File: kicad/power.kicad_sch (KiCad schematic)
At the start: 48 parts, among them J5 Conn_Coaxial_Power, J6 Screw_Terminal_01x02, U11 ADP7118ACPZN, U22 ADP7118ACPZN, U23 LTM8074EY-PBF, U7 LTM8078EY-PBF, U8 ADP7118ACPZN, U9 ADP7118ACPZN

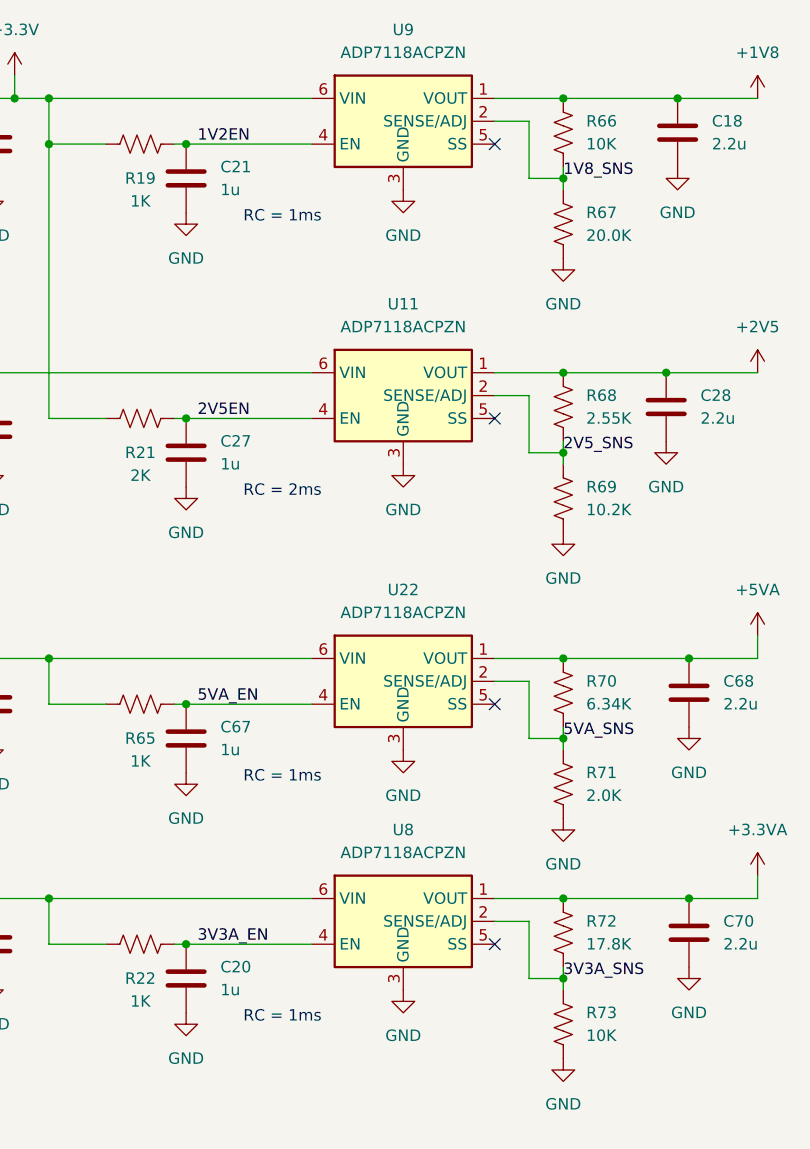
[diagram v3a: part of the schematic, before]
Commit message: fix adc_clk, adp7118
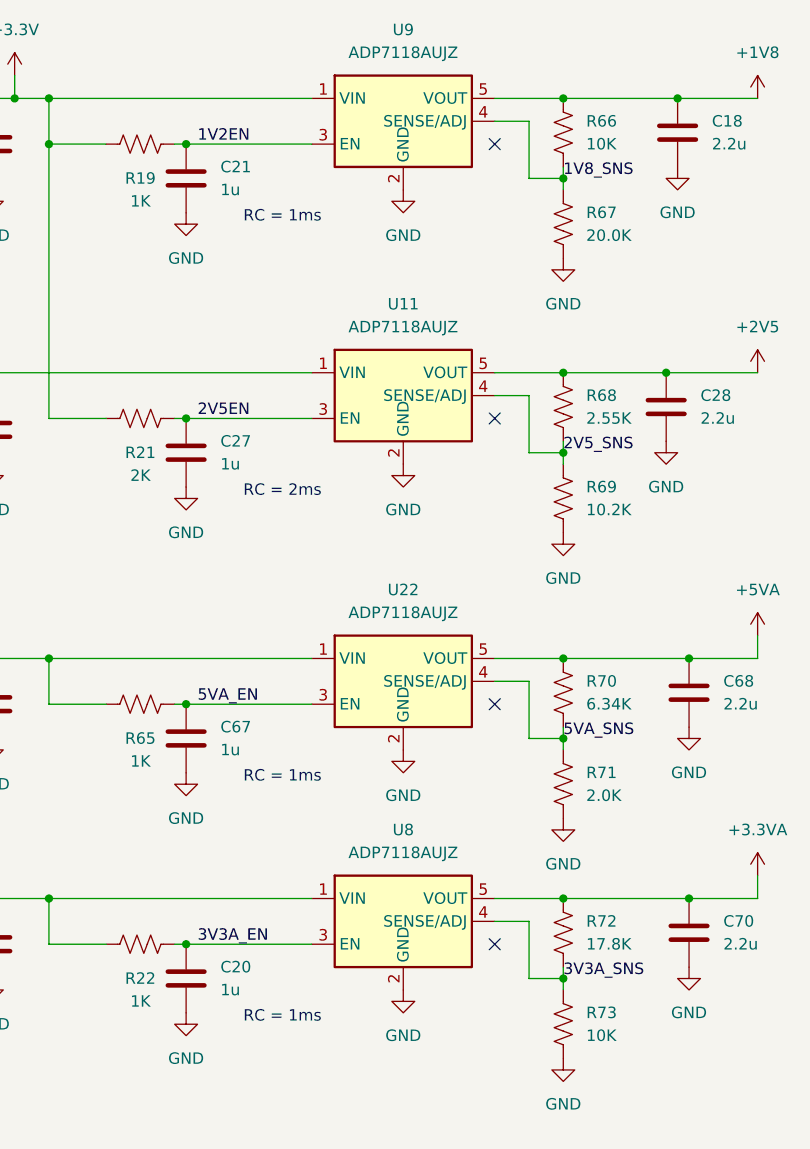
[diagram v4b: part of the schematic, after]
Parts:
- U11, U22, U8, U9: value ADP7118ACPZN -> ADP7118AUJZ; footprint Package_CSP:LFCSP-6-1EP_2x2mm_P0.65mm_EP1x1.6mm -> bgelb_footprint:UJ_5_ADI; symbol Regulator_Linear:ADP7118ACPZN -> bgelb_lib:ADP7118AUJZ
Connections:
- net +1V8: now also U9.5 (VOUT); no longer U9.1 (VOUT)
- net +2V5: now also U11.5 (VOUT); no longer U11.1 (VOUT)
- net +3.3V: now also U11.1 (VIN), U9.1 (VIN); no longer U11.6 (VIN), U9.6 (VIN)
- net +3.3VA: now also U8.5 (VOUT); no longer U8.1 (VOUT)
- net +5VA: now also U22.5 (VOUT); no longer U22.1 (VOUT)
- net 1V2EN: now also U9.3 (EN); no longer U9.4 (EN)
- net 1V8_SNS: now also U9.4 (SENSE/ADJ); no longer U9.2 (SENSE/ADJ)
- net 2V5EN: now also U11.3 (EN); no longer U11.4 (EN)
- net 2V5_SNS: now also U11.4 (SENSE/ADJ); no longer U11.2 (SENSE/ADJ)
- net 3V3A_EN: now also U8.3 (EN); no longer U8.4 (EN)
- net 3V3A_SNS: now also U8.4 (SENSE/ADJ); no longer U8.2 (SENSE/ADJ)
- net 5V5_OUT: now also U22.1 (VIN), U8.1 (VIN); no longer U22.6 (VIN), U8.6 (VIN)
- net 5VA_EN: now also U22.3 (EN); no longer U22.4 (EN)
- net 5VA_SNS: now also U22.4 (SENSE/ADJ); no longer U22.2 (SENSE/ADJ)
- net GND: now also U11.2 (GND), U22.2 (GND), U8.2 (GND), U9.2 (GND); no longer U11.3 (GND), U11.7 (GND), U22.3 (GND), U22.7 (GND), U8.3 (GND), U8.7 (GND), U9.3 (GND), U9.7 (GND)
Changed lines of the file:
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@@
     )
   )
-  (symbol (lib_id "Regulator_Linear:ADP7118ACPZN") (at 302.26 59.69 0) (unit 1)
+  (symbol (lib_id "bgelb_lib:ADP7118AUJZ") (at 302.26 59.69 0) (unit 1)
     (in_bom yes) (on_board yes) (dnp no) (fields_autoplaced)
     (property "Reference" "U9" (at 302.26 49.53 0)
       (effects (font (size 1.27 1.27)))
     )
-    (property "Value" "ADP7118ACPZN" (at 302.26 52.07 0)
-      (effects (font (size 1.27 1.27)))
-    )
-    (property "Footprint" "Package_CSP:LFCSP-6-1EP_2x2mm_P0.65mm_EP1x1.6mm" (at 302.26 72.39 0)
+    (property "Value" "ADP7118AUJZ" (at 302.26 52.07 0)
+      (effects (font (size 1.27 1.27)))
+    )
+    (property "Footprint" "bgelb_footprint:UJ_5_ADI" (at 302.26 72.39 0)
       (effects (font (size 1.27 1.27) italic) hide)
     )
-    (property "Datasheet" "https://www.analog.com/media/en/technical-documentation/data-sheets/ADP7142.pdf" (at 302.26 74.93 0)
+    (property "Datasheet" "https://www.analog.com/media/en/technical-documentation/data-sheets/ADP7118.pdf" (at 302.26 74.93 0)
       (effects (font (size 1.27 1.27)) hide)
     )
     (pin "5")
-    (pin "6")
     (pin "4")
     (pin "3")
     (pin "2")
     (pin "1")
-    (pin "7")
     (instances
       (project "gpsrx"
@@
     )
   )
-  (symbol (lib_id "Regulator_Linear:ADP7118ACPZN") (at 302.26 121.92 0) (unit 1)
+  (symbol (lib_id "bgelb_lib:ADP7118AUJZ") (at 302.26 121.92 0) (unit 1)
     (in_bom yes) (on_board yes) (dnp no) (fields_autoplaced)
     (property "Reference" "U22" (at 302.26 111.76 0)
       (effects (font (size 1.27 1.27)))
     )
-    (property "Value" "ADP7118ACPZN" (at 302.26 114.3 0)
-      (effects (font (size 1.27 1.27)))
-    )
-    (property "Footprint" "Package_CSP:LFCSP-6-1EP_2x2mm_P0.65mm_EP1x1.6mm" (at 302.26 134.62 0)
+    (property "Value" "ADP7118AUJZ" (at 302.26 114.3 0)
+      (effects (font (size 1.27 1.27)))
+    )
+    (property "Footprint" "bgelb_footprint:UJ_5_ADI" (at 302.26 134.62 0)
       (effects (font (size 1.27 1.27) italic) hide)
     )
-    (property "Datasheet" "https://www.analog.com/media/en/technical-documentation/data-sheets/ADP7142.pdf" (at 302.26 137.16 0)
+    (property "Datasheet" "https://www.analog.com/media/en/technical-documentation/data-sheets/ADP7118.pdf" (at 302.26 137.16 0)
       (effects (font (size 1.27 1.27)) hide)
     )
     (pin "5")
-    (pin "6")
     (pin "4")
     (pin "3")
     (pin "2")
     (pin "1")
-    (pin "7")
     (instances
       (project "gpsrx"
@@
     )
   )
-  (symbol (lib_id "Regulator_Linear:ADP7118ACPZN") (at 302.26 148.59 0) (unit 1)
+  (symbol (lib_id "bgelb_lib:ADP7118AUJZ") (at 302.26 148.59 0) (unit 1)
     (in_bom yes) (on_board yes) (dnp no) (fields_autoplaced)
     (property "Reference" "U8" (at 302.26 138.43 0)
       (effects (font (size 1.27 1.27)))
     )
-    (property "Value" "ADP7118ACPZN" (at 302.26 140.97 0)
-      (effects (font (size 1.27 1.27)))
-    )
-    (property "Footprint" "Package_CSP:LFCSP-6-1EP_2x2mm_P0.65mm_EP1x1.6mm" (at 302.26 161.29 0)
+    (property "Value" "ADP7118AUJZ" (at 302.26 140.97 0)
+      (effects (font (size 1.27 1.27)))
+    )
+    (property "Footprint" "bgelb_footprint:UJ_5_ADI" (at 302.26 161.29 0)
       (effects (font (size 1.27 1.27) italic) hide)
     )
-    (property "Datasheet" "https://www.analog.com/media/en/technical-documentation/data-sheets/ADP7142.pdf" (at 302.26 163.83 0)
+    (property "Datasheet" "https://www.analog.com/media/en/technical-documentation/data-sheets/ADP7118.pdf" (at 302.26 163.83 0)
       (effects (font (size 1.27 1.27)) hide)
     )
     (pin "5")
-    (pin "6")
     (pin "4")
     (pin "3")
     (pin "2")
     (pin "1")
-    (pin "7")
     (instances
       (project "gpsrx"
@@
     )
   )
-  (symbol (lib_id "Regulator_Linear:ADP7118ACPZN") (at 302.26 90.17 0) (unit 1)
+  (symbol (lib_id "bgelb_lib:ADP7118AUJZ") (at 302.26 90.17 0) (unit 1)
     (in_bom yes) (on_board yes) (dnp no) (fields_autoplaced)
     (property "Reference" "U11" (at 302.26 80.01 0)
       (effects (font (size 1.27 1.27)))
     )
-    (property "Value" "ADP7118ACPZN" (at 302.26 82.55 0)
-      (effects (font (size 1.27 1.27)))
-    )
-    (property "Footprint" "Package_CSP:LFCSP-6-1EP_2x2mm_P0.65mm_EP1x1.6mm" (at 302.26 102.87 0)
+    (property "Value" "ADP7118AUJZ" (at 302.26 82.55 0)
+      (effects (font (size 1.27 1.27)))
+    )
+    (property "Footprint" "bgelb_footprint:UJ_5_ADI" (at 302.26 102.87 0)
       (effects (font (size 1.27 1.27) italic) hide)
     )
-    (property "Datasheet" "https://www.analog.com/media/en/technical-documentation/data-sheets/ADP7142.pdf" (at 302.26 105.41 0)
+    (property "Datasheet" "https://www.analog.com/media/en/technical-documentation/data-sheets/ADP7118.pdf" (at 302.26 105.41 0)
       (effects (font (size 1.27 1.27)) hide)
     )
     (pin "5")
-    (pin "6")
     (pin "4")
     (pin "3")
     (pin "2")
     (pin "1")
-    (pin "7")
-    (instances
-      (project "gpsrx"
+    (instances
+      (project "gpsrx"
